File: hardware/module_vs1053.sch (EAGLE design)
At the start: 118 parts, among them IC1 IC_USBLC6-2, IC2 LM1117IMPX-3.3, IC3 PIC32MX795F512, IC4 DP83848, IC5 LM1117MPX-2.5, J1 AUDIO_JACK_TRRSSMD_RA, U1 USD-SOCKETUSD, U3 VS1053-L, X2 CRYSTALS-NOGND-CFPX-217, X3 KUSBVX, Y3 CRYSTAL-GROUNDEDSMD-5X3.2

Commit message: Board optimized for SDR (work in progress)
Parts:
- L2: device dp_devices:FERRITE-0805 -> rcl:L-EU0204/7
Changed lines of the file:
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@@
 <part name="GND72" library="supply1" deviceset="GND" device=""/>
 <part name="L1" library="dp_devices" deviceset="FERRITE" device="-0805"/>
-<part name="L2" library="dp_devices" deviceset="FERRITE" device="-0805"/>
+<part name="L2" library="rcl" deviceset="L-EU" device="0204/7"/>
 <part name="GND36" library="supply1" deviceset="GND" device=""/>
 <part name="R21" library="rcl" deviceset="R-EU_" device="R0603"/>
@@
 <instance part="GND72" gate="1" x="-10.16" y="492.76"/>
 <instance part="L1" gate="L" x="68.58" y="561.34" rot="R270"/>
-<instance part="L2" gate="L" x="0" y="523.24" rot="R270"/>
+<instance part="L2" gate="G$1" x="0" y="523.24" rot="R270"/>
 <instance part="GND36" gate="1" x="622.3" y="48.26"/>
 <instance part="R21" gate="G$1" x="624.84" y="60.96" rot="R90"/>
@@
 <net name="VS_CVDD" class="0">
 <segment>
-<pinref part="L2" gate="L" pin="1"/>
-<wire x1="7.62" y1="523.24" x2="10.16" y2="523.24" width="0.1524" layer="91"/>
+<pinref part="L2" gate="G$1" pin="1"/>
+<wire x1="5.08" y1="523.24" x2="10.16" y2="523.24" width="0.1524" layer="91"/>
 <label x="10.16" y="523.24" size="1.4224" layer="95" xref="yes"/>
 </segment>
@@
 <junction x="-10.16" y="508"/>
 <label x="10.16" y="508" size="1.4224" layer="95" xref="yes"/>
-<pinref part="L2" gate="L" pin="2"/>
-<wire x1="-7.62" y1="523.24" x2="-10.16" y2="523.24" width="0.1524" layer="91"/>
+<pinref part="L2" gate="G$1" pin="2"/>
+<wire x1="-5.08" y1="523.24" x2="-10.16" y2="523.24" width="0.1524" layer="91"/>
 <wire x1="-10.16" y1="523.24" x2="-10.16" y2="508" width="0.1524" layer="91"/>
 </segment>

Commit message: ADC (work in progress)
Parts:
- added C61, C62: 10n, rcl:C-EUC0603
- added C63, C64: 1u, rcl:C-EUC0603
- added JP1: (no value), pinhead:PINHD-1X3
- added R12, R37: 470, rcl:R-EU_0204/5
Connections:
- new net IN_LEFT: C63.2, JP1.2
- new net IN_RIGHT: C64.2, JP1.1
- new net N$13: C62.2, R12.2, U3G$1.MICP/LINEINL
- new net N$14: C64.1, R37.1
- new net N$15: C63.1, R12.1
- new net N$5: C61.2, R37.2, U3G$1.LINEINR
- net VS_AGND: now also C61.1, C62.1, JP1.3
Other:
- moved on the sheet: C36, C37, C39, C43, C44, J1, R22, R23, R24, R31, R32, R33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

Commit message: Line input added
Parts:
- R12, R37: device rcl:R-EU_0204/5 -> rcl:R-EU_0204/7
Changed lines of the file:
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@@
 <part name="C61" library="rcl" deviceset="C-EU" device="C0603" value="10n"/>
 <part name="C62" library="rcl" deviceset="C-EU" device="C0603" value="10n"/>
-<part name="R12" library="rcl" deviceset="R-EU_" device="0204/5" value="470"/>
-<part name="R37" library="rcl" deviceset="R-EU_" device="0204/5" value="470"/>
+<part name="R12" library="rcl" deviceset="R-EU_" device="0204/7" value="470"/>
+<part name="R37" library="rcl" deviceset="R-EU_" device="0204/7" value="470"/>
 <part name="C63" library="rcl" deviceset="C-EU" device="C0603" value="1u"/>
 <part name="C64" library="rcl" deviceset="C-EU" device="C0603" value="1u"/>

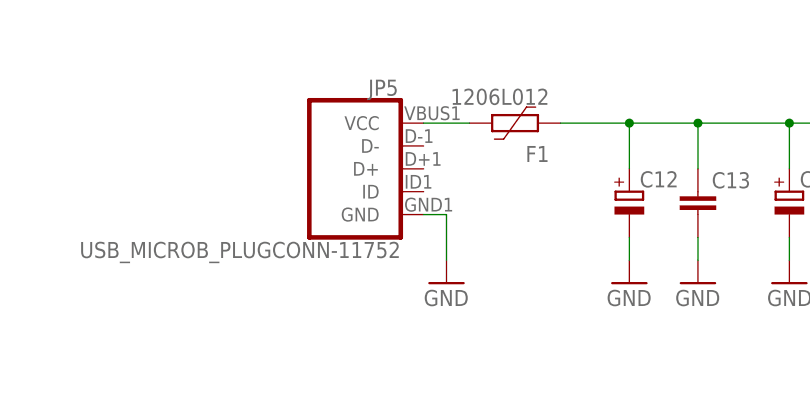
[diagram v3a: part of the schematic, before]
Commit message: Alternate power connector added
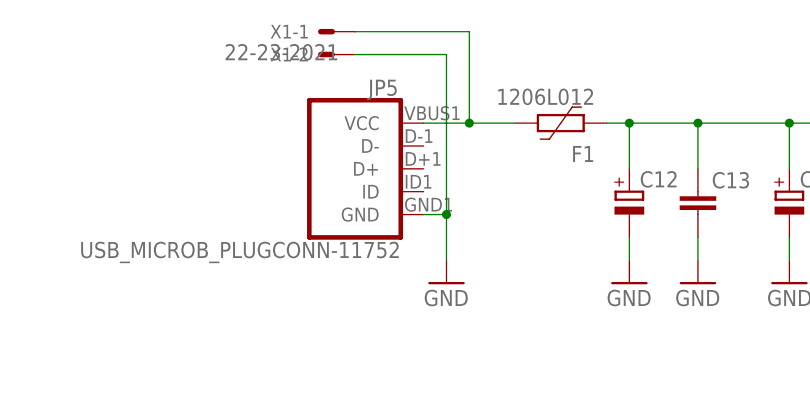
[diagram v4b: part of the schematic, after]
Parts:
- added X1: 22-23-2021, con-molex:22-23-2021
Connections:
- net GND: now also X1-2.S
- net N$17: now also X1-1.S
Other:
- moved on the sheet: F1
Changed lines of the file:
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@@
 <part name="C64" library="rcl" deviceset="C-EU" device="C0603" value="1u"/>
 <part name="JP1" library="pinhead" deviceset="PINHD-1X3" device=""/>
+<part name="X1" library="con-molex" deviceset="22-23-2021" device=""/>
 </parts>
 <sheets>
@@
 <instance part="JP5" gate="G$1" x="-109.22" y="548.64" rot="MR0"/>
 <instance part="GND40" gate="1" x="-99.06" y="535.94"/>
-<instance part="F1" gate="G$1" x="-91.44" y="553.72" rot="R180"/>
+<instance part="F1" gate="G$1" x="-86.36" y="553.72" rot="R180"/>
 <instance part="C30" gate="G$1" x="-60.96" y="546.1"/>
 <instance part="GND49" gate="1" x="-60.96" y="535.94" rot="MR0"/>
@@
 <instance part="C64" gate="G$1" x="551.18" y="139.7" rot="R90"/>
 <instance part="JP1" gate="A" x="571.5" y="142.24"/>
+<instance part="X1" gate="-1" x="-111.76" y="563.88" rot="R180"/>
+<instance part="X1" gate="-2" x="-111.76" y="561.34" rot="R180"/>
 </instances>
 <busses>
@@
 </segment>
 <segment>
+<pinref part="GND40" gate="1" pin="GND"/>
 <pinref part="JP5" gate="G$1" pin="GND"/>
-<pinref part="GND40" gate="1" pin="GND"/>
 <wire x1="-101.6" y1="543.56" x2="-99.06" y2="543.56" width="0.1524" layer="91"/>
 <wire x1="-99.06" y1="543.56" x2="-99.06" y2="538.48" width="0.1524" layer="91"/>
+<pinref part="X1" gate="-2" pin="S"/>
+<wire x1="-109.22" y1="561.34" x2="-99.06" y2="561.34" width="0.1524" layer="91"/>
+<wire x1="-99.06" y1="561.34" x2="-99.06" y2="543.56" width="0.1524" layer="91"/>
+<junction x="-99.06" y="543.56"/>
 </segment>
 <segment>
@@
 <wire x1="-38.1" y1="505.46" x2="-38.1" y2="508" width="0.1524" layer="91"/>
 <junction x="-38.1" y="508"/>
-<wire x1="-86.36" y1="553.72" x2="-78.74" y2="553.72" width="0.1524" layer="91"/>
+<wire x1="-81.28" y1="553.72" x2="-78.74" y2="553.72" width="0.1524" layer="91"/>
 <pinref part="F1" gate="G$1" pin="2"/>
 <pinref part="C12" gate="G$1" pin="+"/>
@@
 <pinref part="F1" gate="G$1" pin="1"/>
 <wire x1="-101.6" y1="553.72" x2="-96.52" y2="553.72" width="0.1524" layer="91"/>
-</segment>
-</net>
+<pinref part="X1" gate="-1" pin="S"/>
+<wire x1="-96.52" y1="553.72" x2="-91.44" y2="553.72" width="0.1524" layer="91"/>
+<wire x1="-109.22" y1="563.88" x2="-96.52" y2="563.88" width="0.1524" layer="91"/>
+<wire x1="-96.52" y1="563.88" x2="-96.52" y2="553.72" width="0.1524" layer="91"/>
+<junction x="-96.52" y="553.72"/>
+</segment>
+</net>
